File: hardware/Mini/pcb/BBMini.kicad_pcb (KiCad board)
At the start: 2 copper layers, 123 x 91 mm, 43 parts, among them J1 Schurter_CMF1, J2 Display, SW1 SW_Push, U1 ESP8266-12E_NodeMCU_Lolin, U2 MCP3208

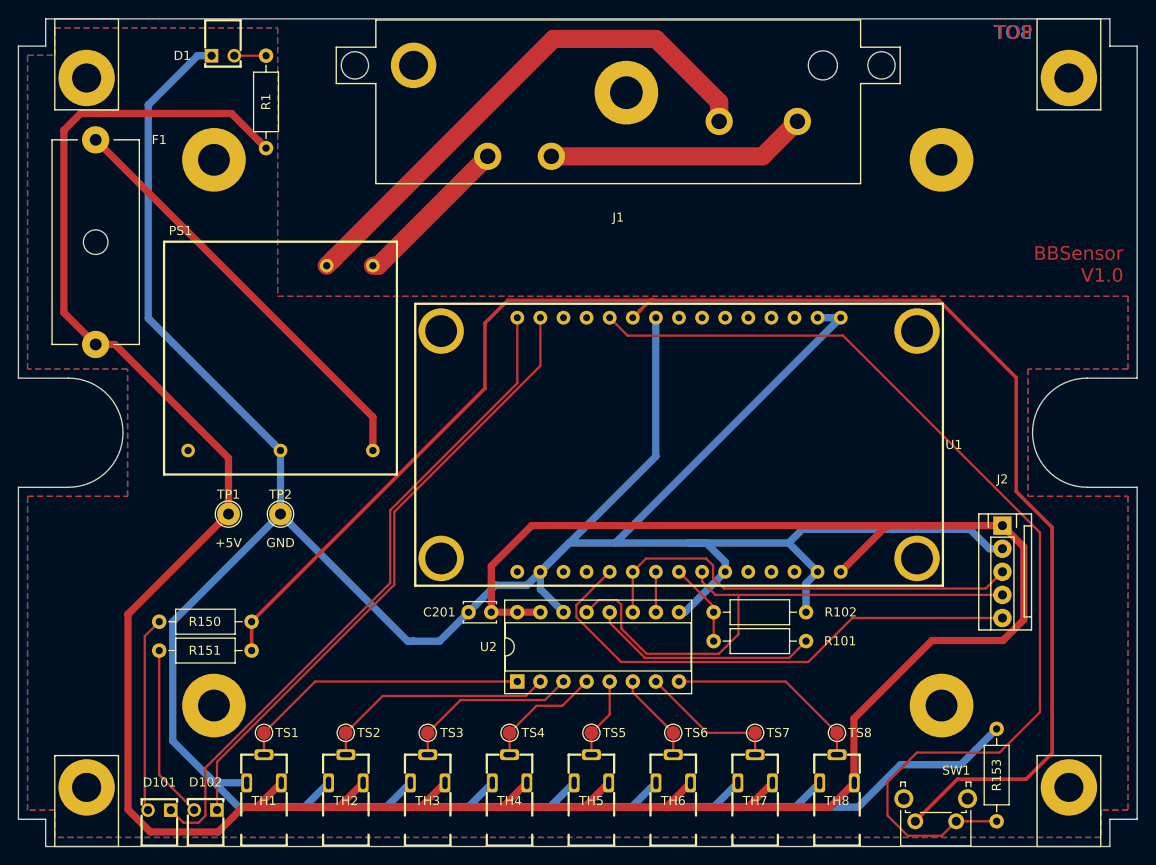
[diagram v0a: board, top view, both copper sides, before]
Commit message: feat: Firmware - Make basics work
switch PINs for SPI Interface

Issue #12
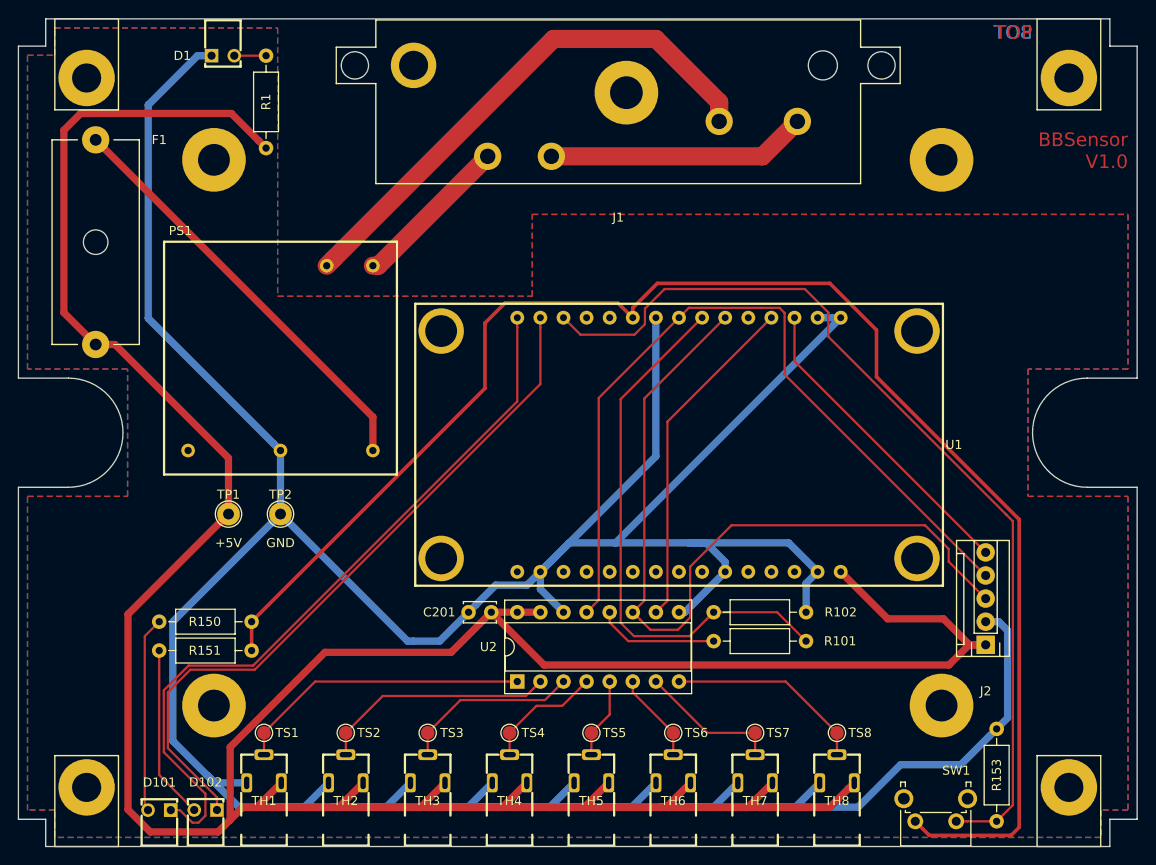
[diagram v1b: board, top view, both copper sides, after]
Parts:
- moved J2 13.2 mm to (121.3, 83.8), turned to 180 degrees
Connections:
- R101 pad 1: /ESP8266/MISO -> /Analog/Digital/SPI2
- R101 pad 2: /Analog/Digital/SPI2 -> /ESP8266/MISO
- U1 pad 18: Net-(U1-Pad18) -> Net-(R153-Pad1)
- U1 pad 20: Net-(R153-Pad1) -> Net-(U1-Pad20)
- U1 pad 23: Net-(U1-Pad23) -> /Analog/Digital/SPI3
- U1 pad 24: Net-(U1-Pad24) -> /ESP8266/MISO
- U1 pad 25: Net-(U1-Pad25) -> /Analog/Digital/SPI1
- U1 pad 27: Net-(U1-Pad27) -> /Analog/Digital/SPI4
- U1 pad 28: Net-(U1-Pad28) -> /Display/SPI5
- U1 pad 5: /Display/SPI5 -> Net-(U1-Pad5)
- U1 pad 6: /Analog/Digital/SPI1 -> Net-(U1-Pad6)
- U1 pad 7: /Analog/Digital/SPI4 -> Net-(U1-Pad7)
- U1 pad 8: /ESP8266/MISO -> Net-(U1-Pad8)
- U1 pad 9: /Analog/Digital/SPI3 -> Net-(U1-Pad9)
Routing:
- net /ESP8266/MISO: track 9.20 -> 60.7 mm
- net /Analog/Digital/SPI1: track 48.6 -> 88.4 mm
- net /Analog/Digital/SPI4: track 4.44 -> 37.6 mm
- net /Analog/Digital/SPI3: track 61.1 -> 86.9 mm
- net /Display/SPI5: track 57.4 -> 34.5 mm
- net /Analog/Digital/SPI2: track 25.1 -> 13.4 mm
- net GND: track 450.0 -> 439.1 mm
- net Net-(R153-Pad1): track 114.0 -> 103.6 mm
- net Net-(D102-Pad1): track 68.9 -> 77.5 mm
- net Net-(D101-Pad1): track 73.7 -> 81.6 mm
- net +5V: track 362.7 -> 367.7 mm
- net +3V3: track 173.7 -> 169.2 mm

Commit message: feat: Firmware - Make basics work
add second push button

Issue #12
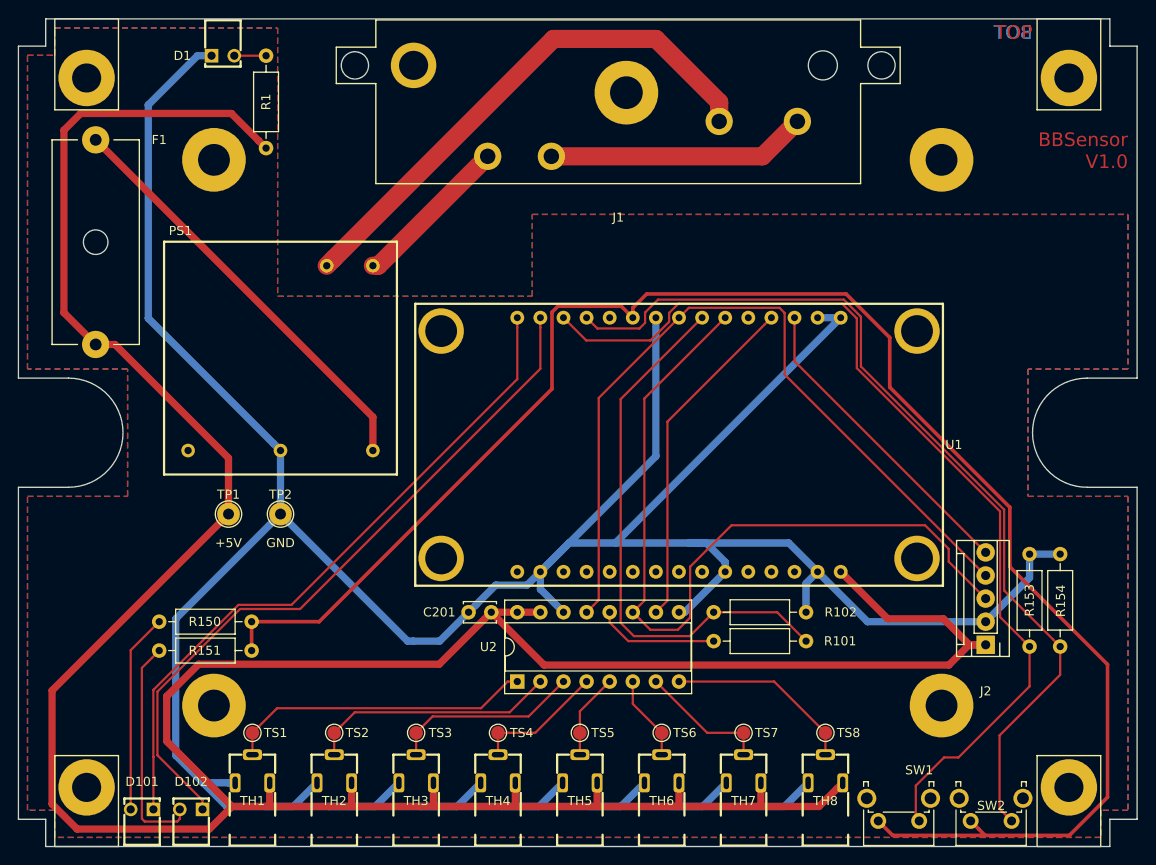
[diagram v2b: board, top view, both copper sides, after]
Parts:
- added R154: 2k2, Resistor_THT:R_Axial_DIN0207_L6.3mm_D2.5mm_P10.16mm_Horizontal, F.Cu at (129.5, 84.0)
- added SW2: SW_Push, Button_Switch_THT:SW_Tactile_SPST_Angled_PTS645Vx83-2LFS, F.Cu at (124.2, 103.2)
- moved R153 19.6 mm to (126.2, 84.0)
- moved SW1 4.07 mm to (114.0, 103.2)
- moved D101 1.91 mm to (28.6, 105.9)
- moved D102 1.59 mm to (34.0, 105.9)
- moved TH1 1.27 mm to (40.7, 105.9)
- moved TH2 1.27 mm to (49.7, 105.9)
- moved TH3 1.27 mm to (58.7, 105.9)
- moved TS1 1.27 mm to (40.7, 93.5)
- moved TS3 1.27 mm to (58.7, 93.5)
- moved TH4 1.27 mm to (67.7, 105.9)
- moved TH5 1.27 mm to (76.7, 105.9)
- moved TH6 1.27 mm to (85.7, 105.9)
- moved TH7 1.27 mm to (94.7, 105.9)
- moved TH8 1.27 mm to (103.7, 105.9)
- moved TS2 1.27 mm to (49.7, 93.5)
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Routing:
- net Net-(R154-Pad1): track 0.00 -> 101.2 mm
- net GND: track 439.1 -> 411.9 mm
- net +3V3: track 169.2 -> 187.2 mm
- net Net-(D101-Pad1): track 81.6 -> 74.1 mm
- net +5V: track 367.7 -> 361.1 mm
- net Net-(D102-Pad2): track 19.1 -> 24.7 mm
- net Net-(R153-Pad1): track 103.6 -> 105.6 mm
- net /Analog/Digital/SIGNAL3: track 19.7 -> 20.9 mm
- net /Analog/Digital/SIGNAL8: track 22.1 -> 20.8 mm
- net /Analog/Digital/SIGNAL7: track 15.6 -> 14.4 mm
- net /Analog/Digital/SIGNAL4: track 13.2 -> 14.5 mm
- net /Analog/Digital/SIGNAL2: track 26.1 -> 27.4 mm
- net /Analog/Digital/SIGNAL1: track 32.6 -> 33.9 mm
- net /Analog/Digital/SIGNAL6: track 9.88 -> 9.36 mm
- net /Analog/Digital/SIGNAL5: track 8.87 -> 9.40 mm

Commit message: feat: Firmware: Add Display
* use correct buttons and LED PINs in PCB

Issue #5
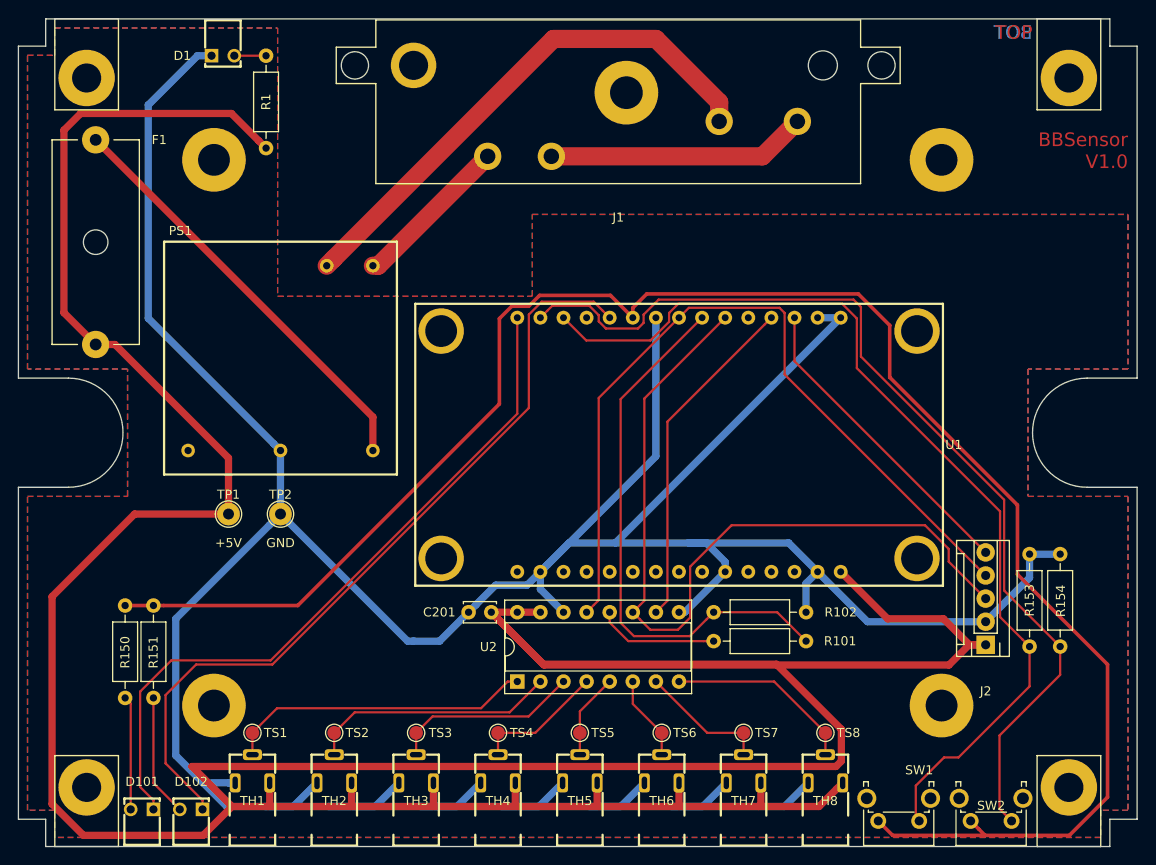
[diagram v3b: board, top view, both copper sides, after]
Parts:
- moved R150 14.0 mm to (26.7, 79.5), turned to 270 degrees
- moved R151 11.9 mm to (29.8, 79.5), turned to 270 degrees
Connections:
- U1 pad 17: Net-(D102-Pad1) -> Net-(R154-Pad1)
- U1 pad 19: Net-(R154-Pad1) -> Net-(U1-Pad19)
- U1 pad 20: Net-(U1-Pad20) -> Net-(D102-Pad1)
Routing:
- net +5V: track 361.1 -> 438.3 mm
- net +3V3: track 187.2 -> 199.5 mm
- net Net-(D102-Pad2): track 24.7 -> 13.5 mm
- net Net-(D102-Pad1): track 77.4 -> 87.7 mm
- net Net-(D101-Pad2): track 21.9 -> 12.5 mm
- net Net-(R154-Pad1): track 101.2 -> 108.3 mm
- net Net-(D101-Pad1): track 74.1 -> 78.2 mm

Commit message: feat: Firmware: Add Display
* update Mini PCB with current hardware implementation

Issue #5
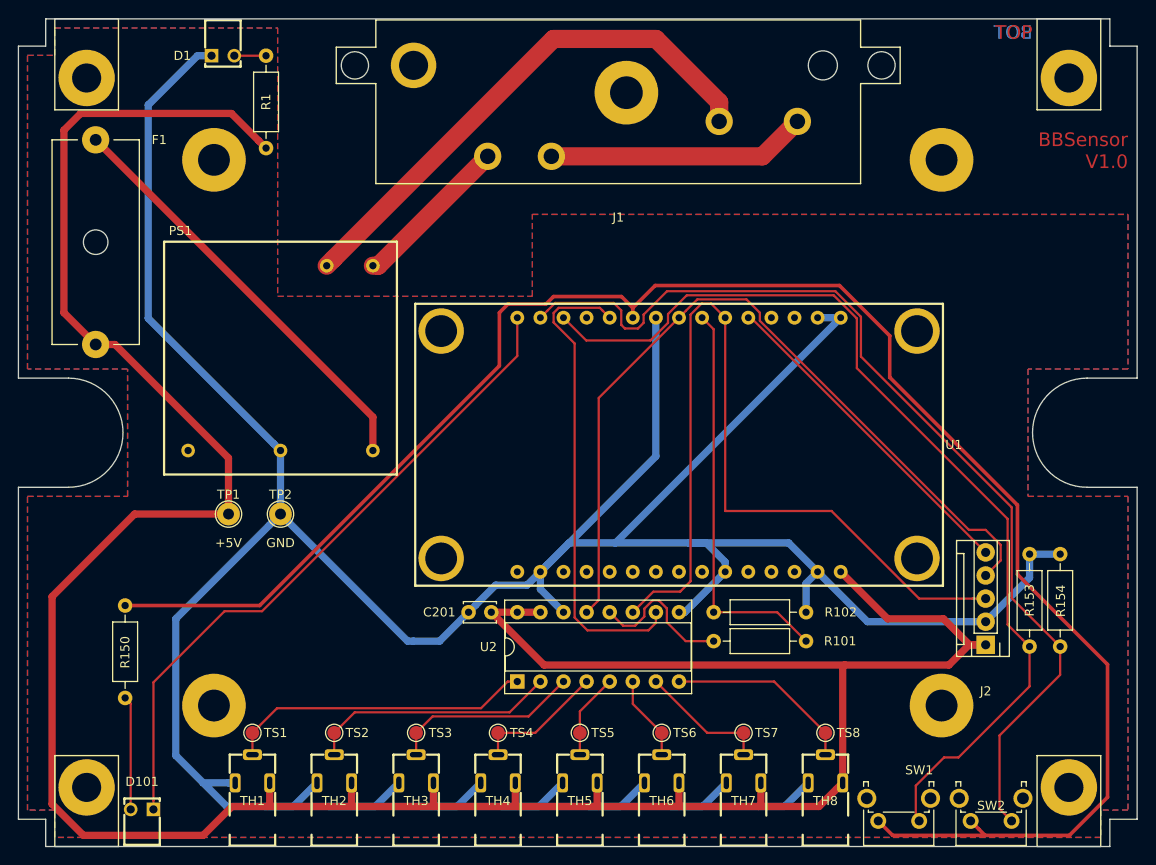
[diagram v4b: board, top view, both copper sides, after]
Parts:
- removed D102: GREEN, VCC:5600F
- removed R151: 140, Resistor_THT:R_Axial_DIN0207_L6.3mm_D2.5mm_P10.16mm_Horizontal
- D101: value RED -> GREEN
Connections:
- U1 pad 20: Net-(D102-Pad1) -> /Analog/Digital/SPI4
- U1 pad 26: Net-(U1-Pad26) -> /Display/SPI5
- U1 pad 27: /Analog/Digital/SPI4 -> Net-(U1-Pad27)
- U1 pad 28: /Display/SPI5 -> Net-(U1-Pad28)
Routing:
- net +5V: track 438.3 -> 326.2 mm
- net Net-(D102-Pad1): track 87.7 -> 0.00 mm
- net /ESP8266/MISO: track 60.7 -> 44.4 mm
- net /Analog/Digital/SPI4: track 37.6 -> 52.3 mm
- net Net-(D102-Pad2): track 13.5 -> 0.00 mm
- net /Analog/Digital/SPI1: track 88.4 -> 95.9 mm
- net Net-(D101-Pad1): track 78.2 -> 73.0 mm
- net /Analog/Digital/SPI2: track 13.4 -> 16.5 mm
- net +3V3: track 199.5 -> 197.0 mm
- net /Display/SPI5: track 34.5 -> 36.8 mm
- net /Analog/Digital/SPI3: track 86.9 -> 88.5 mm
- net Net-(R154-Pad1): track 108.3 -> 109.2 mm
- net Net-(R153-Pad1): track 105.6 -> 106.4 mm

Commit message: feat: Firmware: Add Display
* shrink pcb

Issue #5
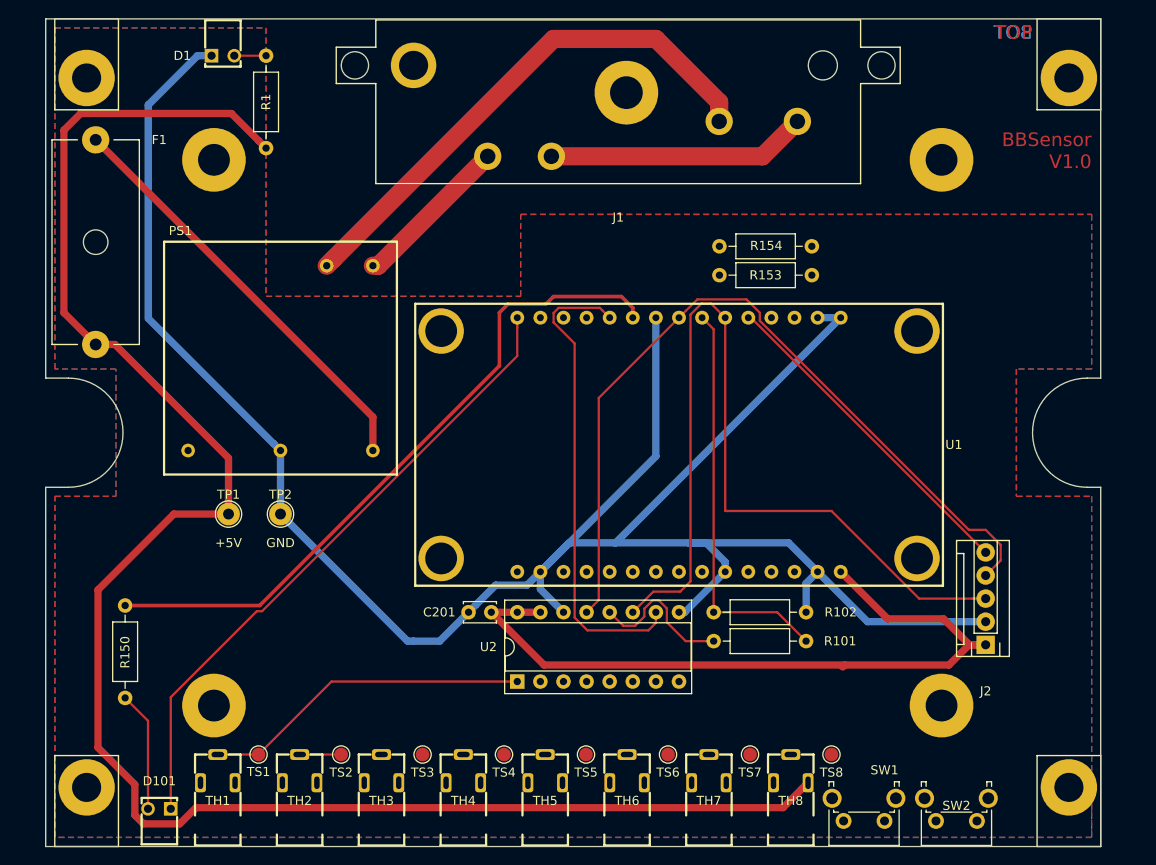
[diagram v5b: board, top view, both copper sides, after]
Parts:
- moved R154 51.8 mm to (102.2, 40.0), turned to 180 degrees
- moved R153 47.3 mm to (102.2, 43.2), turned to 180 degrees
- moved TH4 3.81 mm to (63.9, 105.9)
- moved TH5 3.81 mm to (72.9, 105.9)
- moved TH6 3.81 mm to (81.9, 105.9)
- moved TH7 3.81 mm to (90.9, 105.9)
- moved TH8 3.81 mm to (99.9, 105.9)
- moved TH1 3.81 mm to (36.9, 105.9)
- moved TH2 3.81 mm to (45.9, 105.9)
- moved TH3 3.81 mm to (54.9, 105.9)
- moved SW2 3.81 mm to (120.4, 103.2)
- moved SW1 3.81 mm to (110.2, 103.2)
- moved TS2 2.50 mm to (50.5, 95.9)
- moved TS7 2.49 mm to (95.4, 95.9)
- moved TS3 2.49 mm to (59.4, 95.9)
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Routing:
- net GND: track 411.9 -> 245.8 mm
- net +3V3: track 197.0 -> 74.9 mm
- net Net-(R154-Pad1): track 109.2 -> 0.00 mm
- net Net-(R153-Pad1): track 106.4 -> 0.00 mm
- net +5V: track 326.2 -> 278.7 mm
- net /Analog/Digital/SIGNAL2: track 27.4 -> 4.56 mm
- net /Analog/Digital/SIGNAL3: track 20.9 -> 0.00 mm
- net /Analog/Digital/SIGNAL8: track 20.8 -> 0.00 mm
- net /Analog/Digital/SIGNAL4: track 14.5 -> 0.00 mm
- net /Analog/Digital/SIGNAL7: track 14.4 -> 0.00 mm
- net /Analog/Digital/SIGNAL5: track 9.40 -> 0.00 mm
- net /Analog/Digital/SIGNAL6: track 9.36 -> 0.00 mm
- net Net-(D101-Pad1): track 73.0 -> 70.1 mm
- net /Analog/Digital/SIGNAL1: track 33.9 -> 36.3 mm
- net Net-(D101-Pad2): track 12.5 -> 13.2 mm
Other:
- board size 123 x 91 mm -> 116 x 91 mm

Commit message: feat: Firmware: Add Display
* finish shrinking

Issue #5
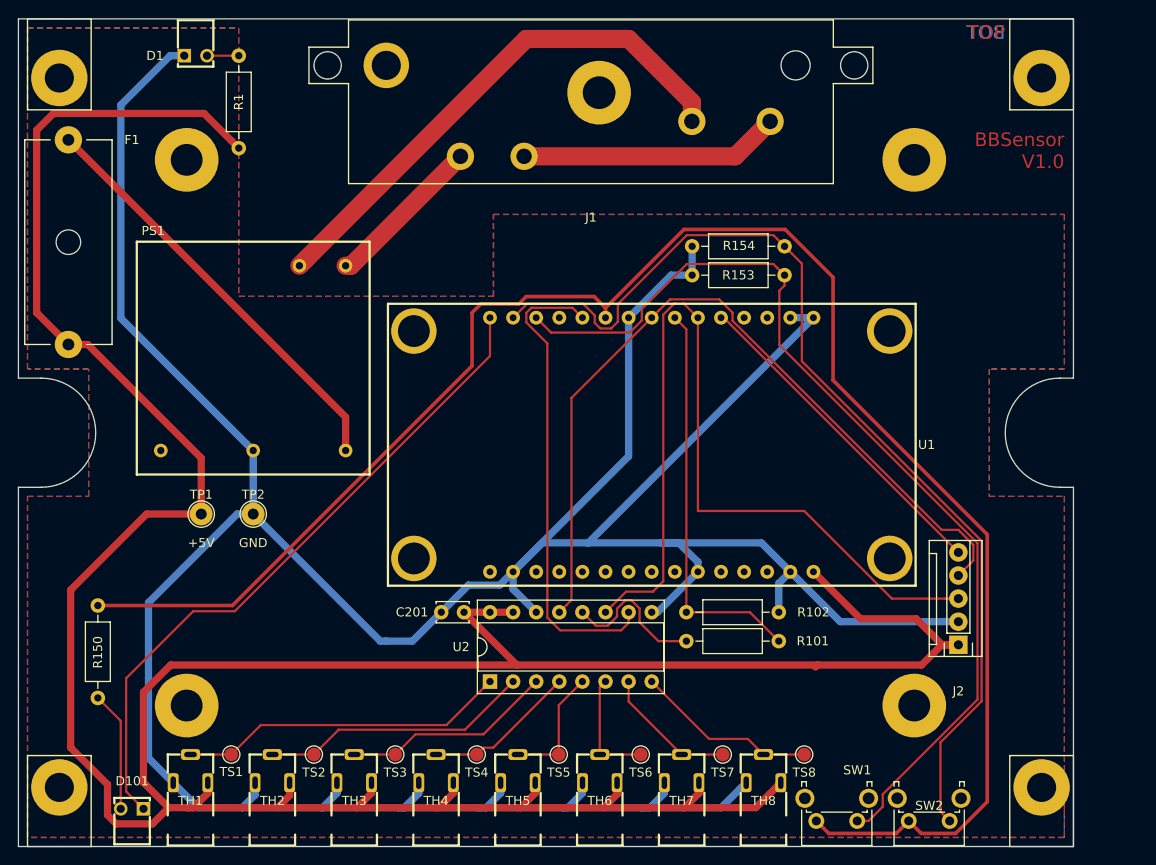
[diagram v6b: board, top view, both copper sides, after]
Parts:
- moved C201 3.00 mm to (64.0, 80.2)
- moved D1 3.00 mm to (34.5, 15.1)
- moved D101 3.00 mm to (27.5, 105.9)
- moved F1 3.00 mm to (20.5, 50.8)
- moved J1 3.00 mm to (77.9, 15.1)
- moved J2 3.00 mm to (118.3, 83.8)
- moved PS1 3.00 mm to (40.8, 52.3)
- moved R1 3.00 mm to (39.2, 19.1)
- moved R101 3.00 mm to (88.4, 83.4)
- moved R102 3.00 mm to (88.4, 80.2)
- moved R150 3.00 mm to (23.7, 79.5)
- moved R153 3.00 mm to (99.2, 43.2)
- moved R154 3.00 mm to (99.2, 40.0)
- moved SW1 3.00 mm to (107.2, 103.2)
- moved SW2 3.00 mm to (117.4, 103.2)
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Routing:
- net GND: track 245.8 -> 383.2 mm
- net +3V3: track 74.9 -> 192.3 mm
- net Net-(R154-Pad1): track 0.00 -> 112.4 mm
- net Net-(R153-Pad1): track 0.00 -> 107.8 mm
- net +5V: track 278.7 -> 360.2 mm
- net /Analog/Digital/SIGNAL2: track 4.56 -> 29.8 mm
- net /Analog/Digital/SIGNAL3: track 0.00 -> 23.3 mm
- net /Analog/Digital/SIGNAL8: track 0.00 -> 20.1 mm
- net /Analog/Digital/SIGNAL4: track 0.00 -> 16.9 mm
- net /Analog/Digital/SIGNAL7: track 0.00 -> 15.0 mm
- net /Analog/Digital/SIGNAL5: track 0.00 -> 13.6 mm
- net /Analog/Digital/SIGNAL6: track 0.00 -> 12.8 mm
- net Net-(D101-Pad1): track 70.1 -> 74.0 mm

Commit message: feat Firmware: Convert Temperatures
update schemes

Issue #27
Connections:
- net Net-(D101-Pad1) renamed /ESP8266/LED
- net Net-(R153-Pad1) renamed /ESP8266/BUTTON1
- net Net-(R154-Pad1) renamed /ESP8266/BUTTON2
